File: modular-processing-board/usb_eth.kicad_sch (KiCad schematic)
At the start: 10 parts, among them J801 TYPE-C-31-M-12

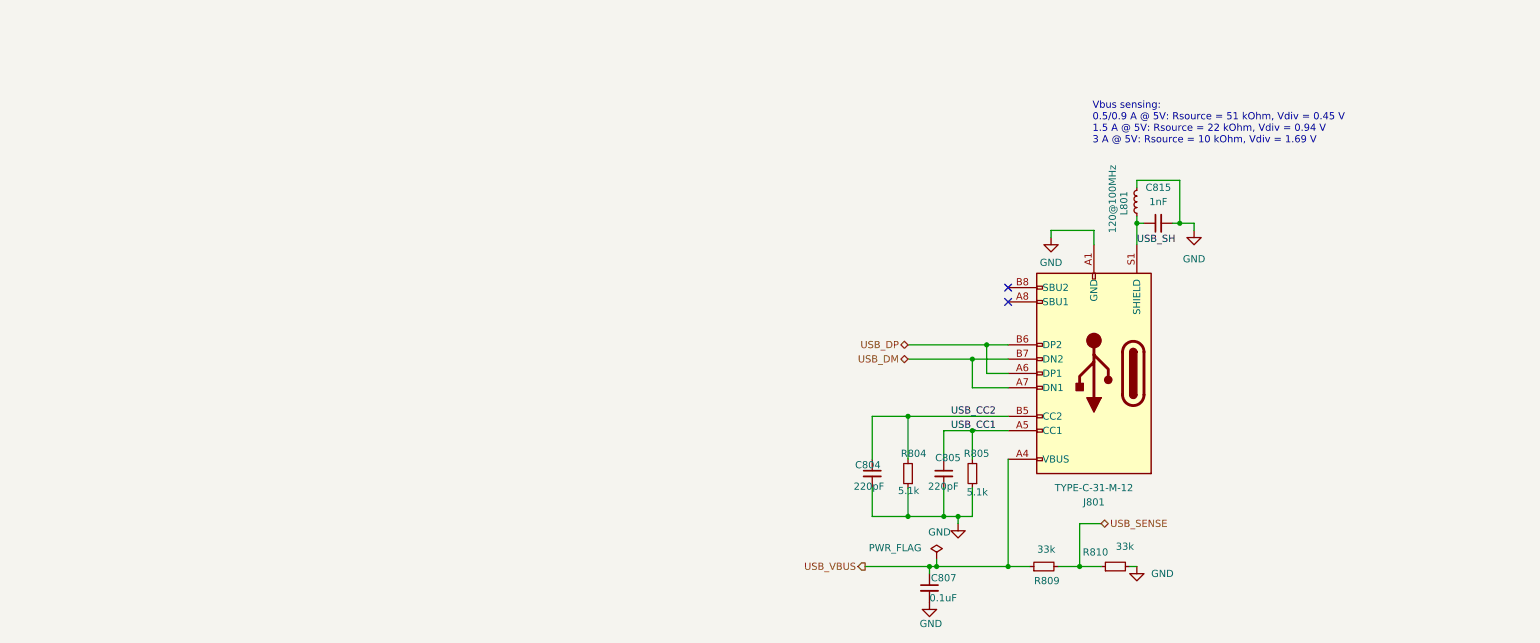
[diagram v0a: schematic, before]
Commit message: added ESD protection,  USB connector, SD-CARD, decoupling caps (next) add appropriate VREF, COAX for ADC, board2board connectors and connect wiring
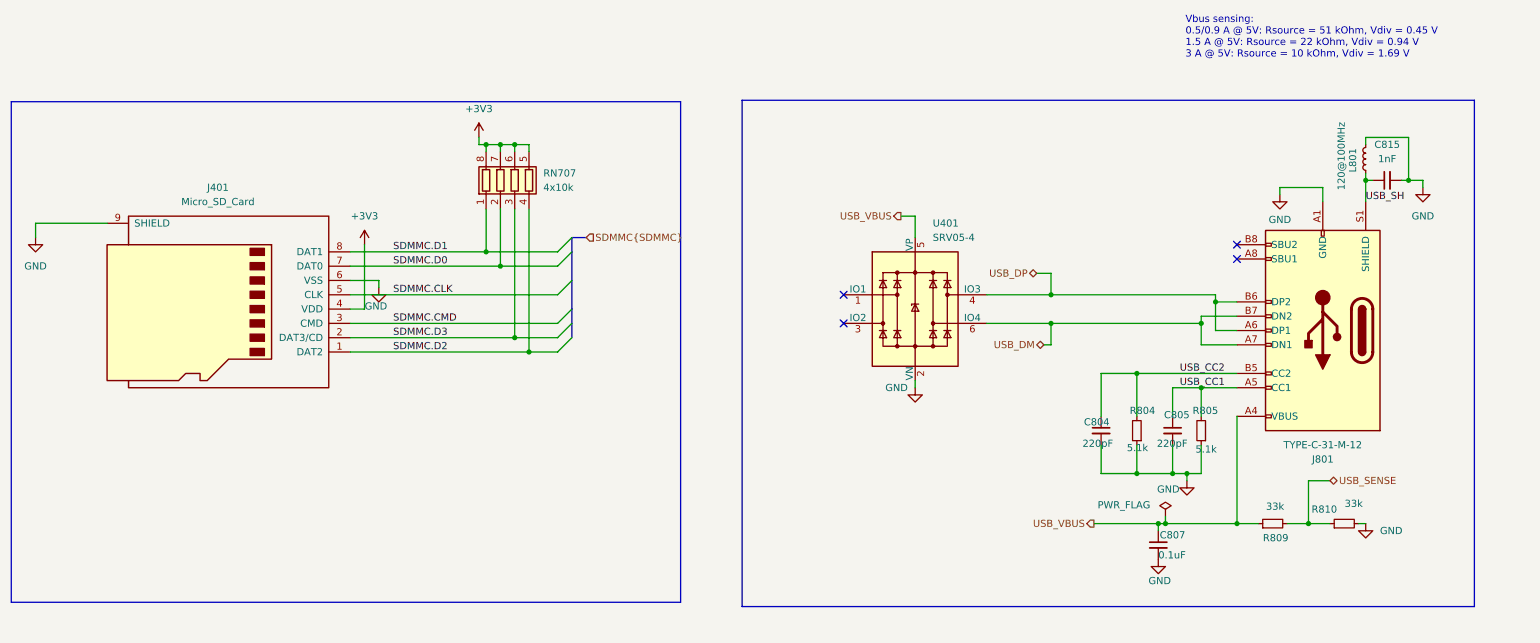
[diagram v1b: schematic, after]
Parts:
- added J401: Micro_SD_Card, iw-memory:TF01A, symbol Connector:Micro_SD_Card
- added RN707: 4x10k, Resistor_SMD:R_Array_Convex_4x0603, symbol Device:R_Pack04
- added U401: SRV05-4, Package_TO_SOT_SMD:SOT-23-6, symbol Power_Protection:SRV05-4
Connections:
- net GND: now also J401.6 (VSS), J401.9 (SHIELD), U401.2 (VN)
- net USB_DM: now also U401.6 (IO4)
- net USB_DP: now also U401.4 (IO3)
- net USB_VBUS: now also U401.5 (VP)
- new net +3V3: J401.4 (VDD), RN707.5 (R4.2), RN707.6 (R3.2), RN707.7 (R2.2), RN707.8 (R1.2)
- new net SDMMC.CLK: J401.5 (CLK)
- new net SDMMC.CMD: J401.3 (CMD)
- new net SDMMC.D0: J401.7 (DAT0), RN707.2 (R2.1)
- new net SDMMC.D1: J401.8 (DAT1), RN707.1 (R1.1)
- new net SDMMC.D2: J401.1 (DAT2), RN707.4 (R4.1)
- new net SDMMC.D3: J401.2 (DAT3/CD), RN707.3 (R3.1)
- no-connect marks 2 -> 4
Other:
- moved on the sheet: C804, C805, C807, C815, J801, L801, R804, R805, R809, R810

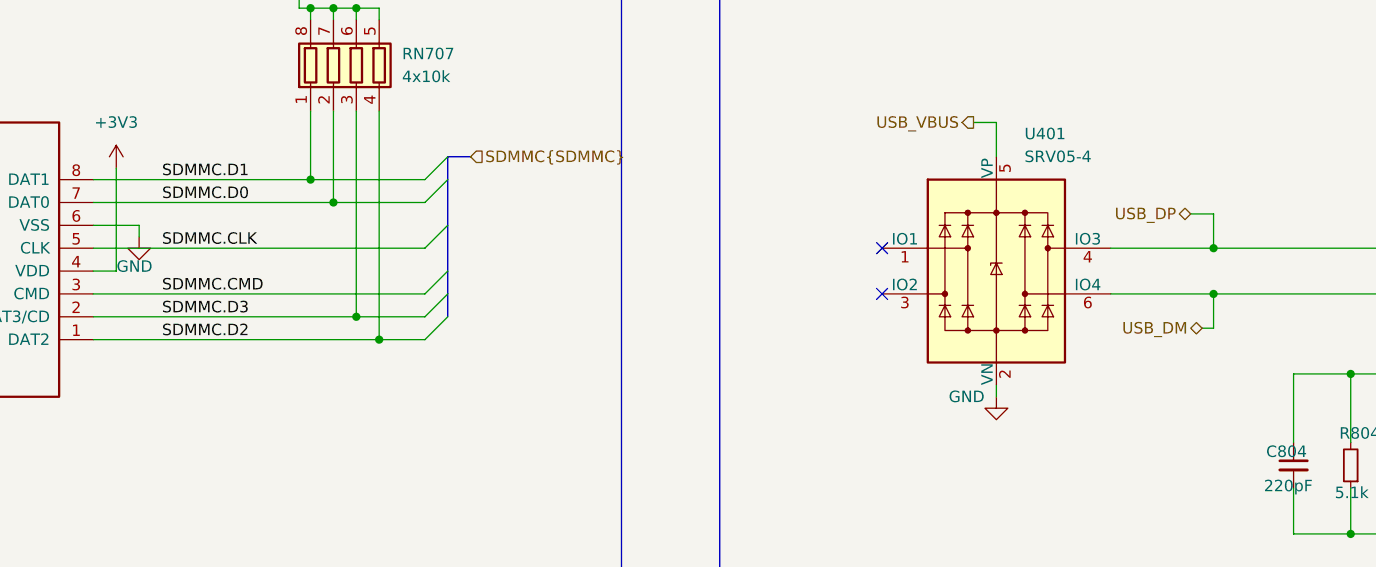
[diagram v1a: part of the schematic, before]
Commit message: Finished basic HW (next) Fix-up all labeling, then start laying out
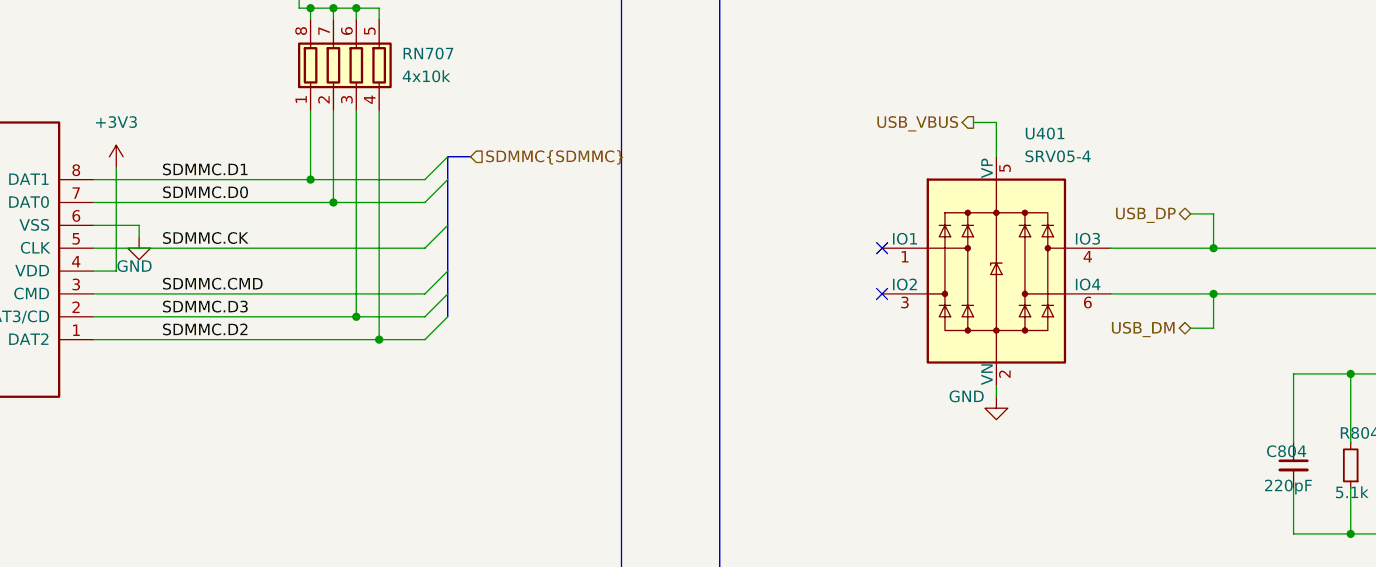
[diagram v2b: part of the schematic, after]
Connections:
- net SDMMC.CLK renamed SDMMC.CK
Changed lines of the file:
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@@
 	(wire
 		(pts
-			(xy 203.2 78.74) (xy 204.47 78.74)
+			(xy 201.93 78.74) (xy 204.47 78.74)
 		)
 		(stroke
@@
 		)
 	)
-	(label "SDMMC.CLK"
+	(label "SDMMC.CK"
 		(at 87.63 69.85 0)
 		(effects
@@
 	(hierarchical_label "USB_DM"
 		(shape bidirectional)
-		(at 203.2 78.74 180)
-		(effects
-			(font
+		(at 201.93 78.74 180)
+		(effects
+			(font

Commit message: completed schematic
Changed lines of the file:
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@@
-		(color 0 0 0 0)
-	)
-	(junction
-		(at 224.79 110.49)
-		(diameter 0)
 		(color 0 0 0 0)
 	)
@@
 	(wire
 		(pts
-			(xy 224.79 110.49) (xy 223.52 110.49)
+			(xy 223.52 110.49) (xy 237.49 110.49)
 		)
 		(stroke
@@
 	(wire
 		(pts
-			(xy 224.79 110.49) (xy 237.49 110.49)
-		)
-		(stroke
-			(width 0)
-			(type default)
-		)
-	)
-	(wire
-		(pts
 			(xy 104.14 43.18) (xy 104.14 44.45)
 		)
@@
 		(pts
 			(xy 119.38 59.69) (xy 119.38 62.23)
-		)
-		(stroke
-			(width 0)
-			(type default)
-		)
-	)
-	(wire
-		(pts
-			(xy 224.79 110.49) (xy 224.79 109.22)
 		)
 		(stroke
@@
 					(unit 1)
 				)
-			)
-		)
-	)
-	(symbol
-		(lib_id "power:PWR_FLAG")
-		(at 224.79 109.22 0)
-		(unit 1)
-		(exclude_from_sim no)
-		(in_bom yes)
-		(on_board yes)
-		(dnp no)
-		(property "Reference" "#FLG0801"
-			(at 224.79 107.315 0)
-			(effects
-				(font
-					(size 1.27 1.27)
-				)
-				(hide yes)
-			)
-		)
-		(property "Value" "PWR_FLAG"
-			(at 217.424 107.188 0)
-			(effects
-				(font
-					(size 1.27 1.27)
-				)
-			)
-		)
-		(property "Footprint" ""
-			(at 224.79 109.22 0)
-			(effects
-				(font
-					(size 1.27 1.27)
-				)
-				(hide yes)
-			)
-		)
-		(property "Datasheet" "~"
-			(at 224.79 109.22 0)
-			(effects
-				(font
-					(size 1.27 1.27)
-				)
-				(hide yes)
-			)
-		)
-		(property "Description" "Special symbol for telling ERC where power comes from"
-			(at 224.79 109.22 0)
-			(effects
-				(font
-					(size 1.27 1.27)
-				)
-				(hide yes)
-			)
-		)
-		(pin "1"
-		)
-		(instances
-			(project "modular-processing-board"
-				(path "/73b5a92f-908b-4f97-a96c-14ee20a7f293/5a39632a-7d64-4b17-8b3b-2384b46c7599"
-					(reference "#FLG0801")
-					(unit 1)
-				)

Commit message: various changes to schematic (next) add bias resistors after testing results on acoustic-carrier-board
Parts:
- C807: footprint Capacitor_SMD:C_0201_0603Metric -> Capacitor_SMD:C_0402_1005Metric; LPN (none) -> C307331; MPN (none) -> CL05B104KB54PNC
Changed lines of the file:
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@@
 			)
 		)
-		(property "Footprint" "Capacitor_SMD:C_0201_0603Metric"
+		(property "Footprint" "Capacitor_SMD:C_0402_1005Metric"
 			(at 223.52 114.3 0)
 			(effects
@@
 			(at 223.52 114.3 0)
 			(effects
+				(font
+					(size 1.27 1.27)
+				)
+				(hide yes)
+			)
+		)
+		(property "LPN" "C307331"
+			(at 223.52 114.3 0)
+			(effects
+				(font
+					(size 1.27 1.27)
+				)
+				(hide yes)
+			)
+		)
+		(property "MPN" "CL05B104KB54PNC"
+			(at 223.52 114.3 0)
+			(effects

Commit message: replaced sdmmc connector, added smmc trace, added u.fl. connectors
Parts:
- removed J401: Micro_SD_Card, iw-memory:TF01A, symbol Connector:Micro_SD_Card
- added C401: 0.1uF, Capacitor_SMD:C_0402_1005Metric, symbol Device:C_Small
- added J401: TF01A, iw-memory:TF01A, symbol iw-memory:TF01A
- added R401: 10k, Resistor_SMD:R_0603_1608Metric, symbol Device:R_Small
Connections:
- net +3V3: now also C401.1, J401.4 (VDD), R401.2
- net GND: now also C401.2, J401.10 (MP), J401.6 (VSS)
- net SDMMC.CK: now also J401.5 (CLK)
- net SDMMC.CMD: now also J401.3 (CMD)
- net SDMMC.D0: now also J401.7 (DAT0)
- net SDMMC.D1: now also J401.8 (DAT1)
- net SDMMC.D2: now also J401.1 (DAT2)
- net SDMMC.D3: now also J401.2 (DAT3/CD)
- net USB_DM renamed USB_DN
- new net SDMMC.CD: J401.9 (CD), R401.1
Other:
- moved on the sheet: RN707

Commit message: completed schematic + layout (next) do footprint checks etc.
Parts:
- added TP402, TP403, TP404: TestPoint, iw-misc:TestPoint_Pad_D0.5mm, symbol Connector:TestPoint
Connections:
- net USB_CC1: now also TP403.1
- net USB_CC2: now also TP402.1
- net USB_VBUS: now also TP404.1
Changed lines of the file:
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@@
 	)
 	(junction
+		(at 224.79 110.49)
+		(diameter 0)
+		(color 0 0 0 0)
+	)
+	(junction
 		(at 219.71 101.6)
 		(diameter 0)
@@
 	)
 	(junction
+		(at 213.36 83.82)
+		(diameter 0)
+		(color 0 0 0 0)
+	)
+	(junction
 		(at 81.28 80.01)
 		(diameter 0)
@@
 		(color 0 0 0 0)
 	)
+	(junction
+		(at 226.06 86.36)
+		(diameter 0)
+		(color 0 0 0 0)
+	)
 	(no_connect
 		(at 167.64 74.93)
@@
 	(wire
 		(pts
-			(xy 223.52 110.49) (xy 237.49 110.49)
+			(xy 223.52 110.49) (xy 224.79 110.49)
 		)
 		(stroke
@@
 	(wire
 		(pts
+			(xy 224.79 110.49) (xy 237.49 110.49)
+		)
+		(stroke
+			(width 0)
+			(type default)
+		)
+	)
+	(wire
+		(pts
 			(xy 78.74 87.63) (xy 83.82 87.63)
 		)
@@
 	)
 	(symbol
+		(lib_id "Connector:TestPoint")
+		(at 224.79 110.49 0)
+		(unit 1)
+		(exclude_from_sim no)
+		(in_bom yes)
+		(on_board yes)
+		(dnp no)
+		(fields_autoplaced yes)
+		(property "Reference" "TP404"
+			(at 227.33 105.9179 0)
+			(effects
+				(font
+					(size 1.27 1.27)
+				)
+				(justify left)
+			)
+		)
+		(property "Value" "TestPoint"
+			(at 227.33 108.4579 0)
+			(effects
+				(font
+					(size 1.27 1.27)
+				)
+				(justify left)
+			)
+		)
+		(property "Footprint" "iw-misc:TestPoint_Pad_D0.5mm"
+			(at 229.87 110.49 0)
+			(effects
+				(font
+					(size 1.27 1.27)
+				)
+				(hide yes)
+			)
+		)
+		(property "Datasheet" "~"
+			(at 229.87 110.49 0)
+			(effects
+				(font
+					(size 1.27 1.27)
+				)
+				(hide yes)
+			)
+		)
+		(property "Description" "test point"
+			(at 224.79 110.49 0)
+			(effects
+				(font
+					(size 1.27 1.27)
+				)
+				(hide yes)
+			)
+		)
+		(pin "1"
+		)
+		(instances
+			(project "modular-processing-board"
+				(path "/73b5a92f-908b-4f97-a96c-14ee20a7f293/5a39632a-7d64-4b17-8b3b-2384b46c7599"
+					(reference "TP404")
+					(unit 1)
+				)
+			)
+		)
+	)
+	(symbol
 		(lib_id "Device:R_Small")
 		(at 243.84 110.49 90)
@@
 	)
 	(symbol
+		(lib_id "Connector:TestPoint")
+		(at 226.06 86.36 0)
+		(unit 1)
+		(exclude_from_sim no)
+		(in_bom yes)
+		(on_board yes)
+		(dnp no)
+		(fields_autoplaced yes)
+		(property "Reference" "TP403"
+			(at 228.6 81.7879 0)
+			(effects
+				(font
+					(size 1.27 1.27)
+				)
+				(justify left)
+			)
+		)
+		(property "Value" "TestPoint"
+			(at 228.6 84.3279 0)
+			(effects
+				(font
+					(size 1.27 1.27)
+				)
+				(justify left)
+			)
+		)
+		(property "Footprint" "iw-misc:TestPoint_Pad_D0.5mm"
+			(at 231.14 86.36 0)
+			(effects
+				(font
+					(size 1.27 1.27)
+				)
+				(hide yes)
+			)
+		)
+		(property "Datasheet" "~"
+			(at 231.14 86.36 0)
+			(effects
+				(font
+					(size 1.27 1.27)
+				)
+				(hide yes)
+			)
+		)
+		(property "Description" "test point"
+			(at 226.06 86.36 0)
+			(effects
+				(font
+					(size 1.27 1.27)
+				)
+				(hide yes)
+			)
+		)
+		(pin "1"
+		)
+		(instances
+			(project "modular-processing-board"
+				(path "/73b5a92f-908b-4f97-a96c-14ee20a7f293/5a39632a-7d64-4b17-8b3b-2384b46c7599"
+					(reference "TP403")
+					(unit 1)
+				)
+			)
+		)
+	)
+	(symbol
 		(lib_id "Device:C_Small")
 		(at 226.06 93.98 0)
@@
 					(unit 1)
 				)
+			)
+		)
+	)
+	(symbol
+		(lib_id "Connector:TestPoint")
+		(at 213.36 83.82 0)
+		(unit 1)
+		(exclude_from_sim no)
+		(in_bom yes)
+		(on_board yes)
+		(dnp no)
+		(fields_autoplaced yes)
+		(property "Reference" "TP402"
+			(at 215.9 79.2479 0)
+			(effects
+				(font
+					(size 1.27 1.27)
+				)
+				(justify left)
+			)
+		)
+		(property "Value" "TestPoint"
+			(at 215.9 81.7879 0)
+			(effects
+				(font
+					(size 1.27 1.27)
+				)
+				(justify left)
+			)
+		)
+		(property "Footprint" "iw-misc:TestPoint_Pad_D0.5mm"
+			(at 218.44 83.82 0)
+			(effects
+				(font
+					(size 1.27 1.27)
+				)
+				(hide yes)
+			)
+		)
+		(property "Datasheet" "~"
+			(at 218.44 83.82 0)
+			(effects
+				(font
+					(size 1.27 1.27)
+				)
+				(hide yes)
+			)
+		)
+		(property "Description" "test point"
+			(at 213.36 83.82 0)
+			(effects
+				(font
+					(size 1.27 1.27)
+				)
+				(hide yes)
+			)
+		)
+		(pin "1"
+		)
+		(instances
+			(project "modular-processing-board"
+				(path "/73b5a92f-908b-4f97-a96c-14ee20a7f293/5a39632a-7d64-4b17-8b3b-2384b46c7599"
+					(reference "TP402")
+					(unit 1)
+				)

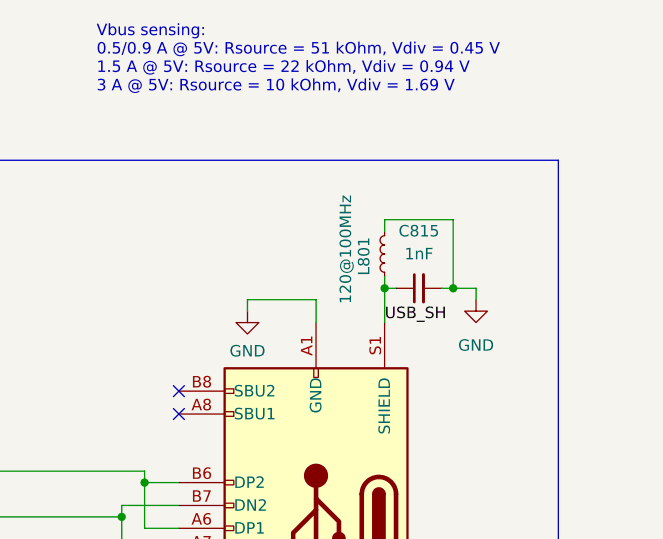
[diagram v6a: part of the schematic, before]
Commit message: checking SDMMC SD-card interface (next) finish checking sd-card holder, check connectors, frontend and power
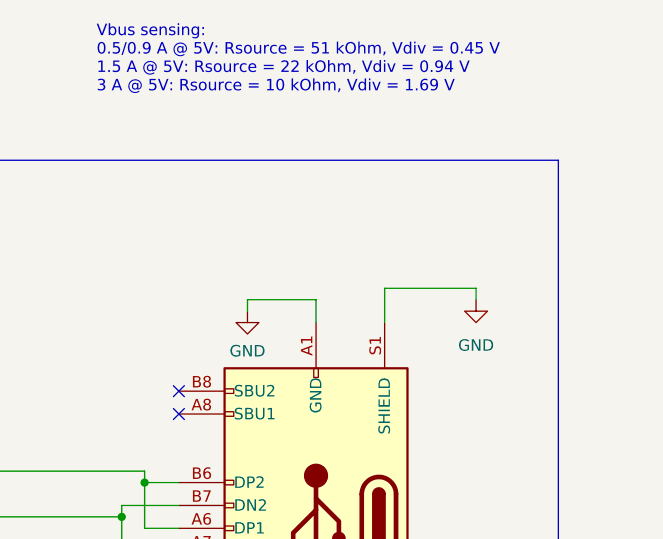
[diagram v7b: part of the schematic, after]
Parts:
- removed C815: 1nF, Capacitor_SMD:C_1206_3216Metric, symbol Device:C_Small
- removed L801: 120@100MHz, Inductor_SMD:L_0603_1608Metric, symbol Device:L_Small
- C401, C807: LCSC Part Number C22435929 -> (none); Manufacturing Part Number CGA0201X7R104K160ET -> (none)
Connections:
- net USB_SH is gone; now on net GND: J801.S1 (SHIELD)

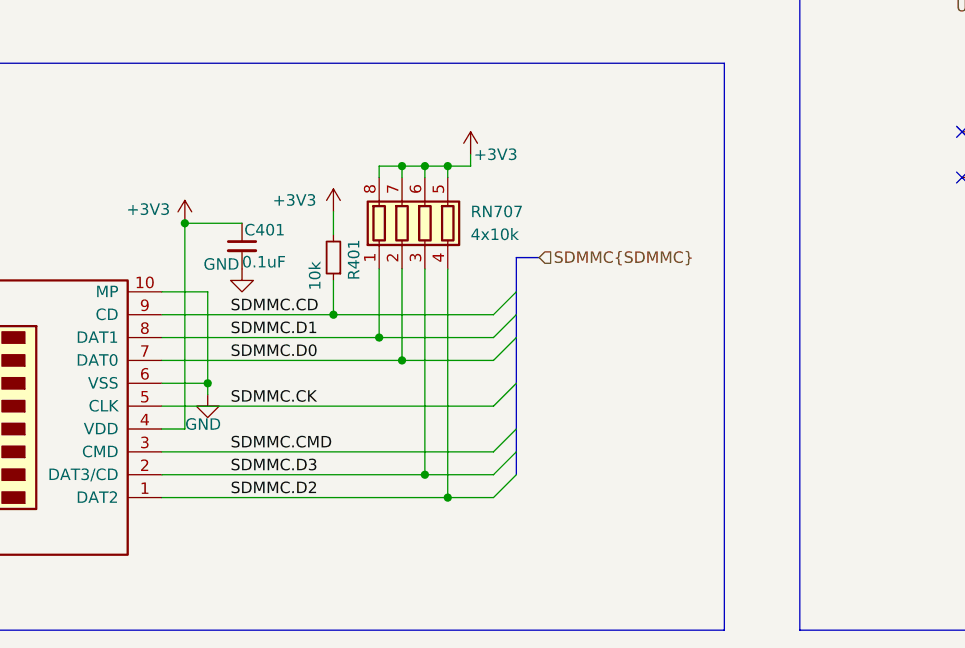
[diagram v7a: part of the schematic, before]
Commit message: finished schematic checks, added extra capacitors on LDO output (next) add holes to board / board shape, do layout checks
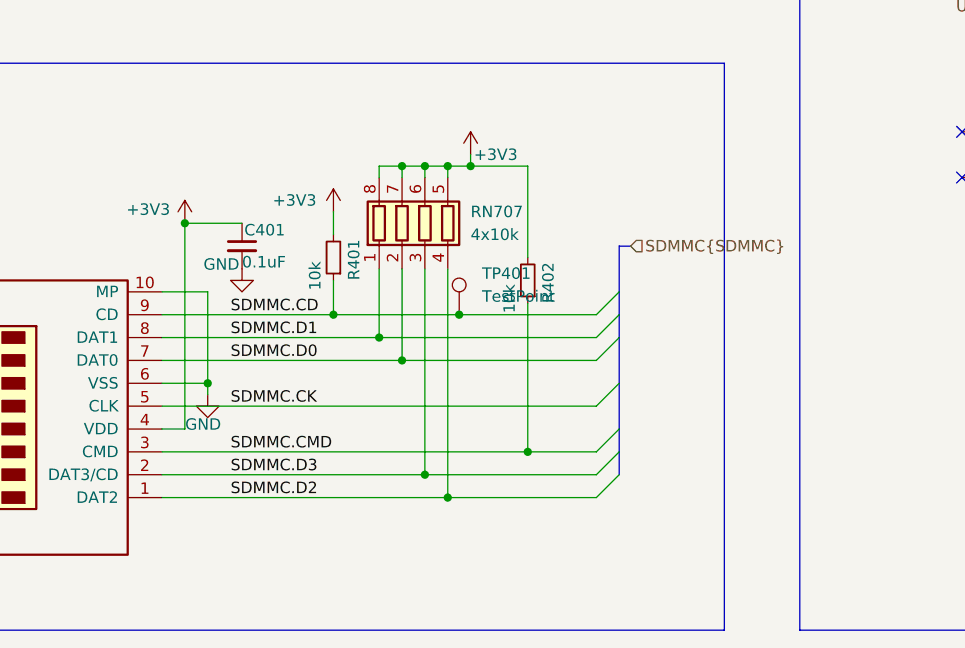
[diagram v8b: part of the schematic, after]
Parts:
- added R402: 10k, Resistor_SMD:R_0603_1608Metric, symbol Device:R_Small
- added TP401: TestPoint, iw-misc:TestPoint_Pad_D0.5mm, symbol Connector:TestPoint
- J401: LPN (none) -> C2889258; MPN (none) -> TF-01A
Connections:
- net +3V3: now also R402.2
- net SDMMC.CD: now also TP401.1
- net SDMMC.CMD: now also R402.1
